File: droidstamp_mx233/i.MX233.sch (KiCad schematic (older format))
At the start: 91 parts, among them IC1 iMX233, J1 MICROSD, J5 JACK-PLUG, P1 CONN_12X2, P10 CONN_1, P2 CONN_12X2, P3 CONN_1, P4 CONN_4X2, P5 CONN_1, P7 CONN_1, Q1 MMDT3904, U1 ADM3101E, U3 M25P32, X1 24MHz

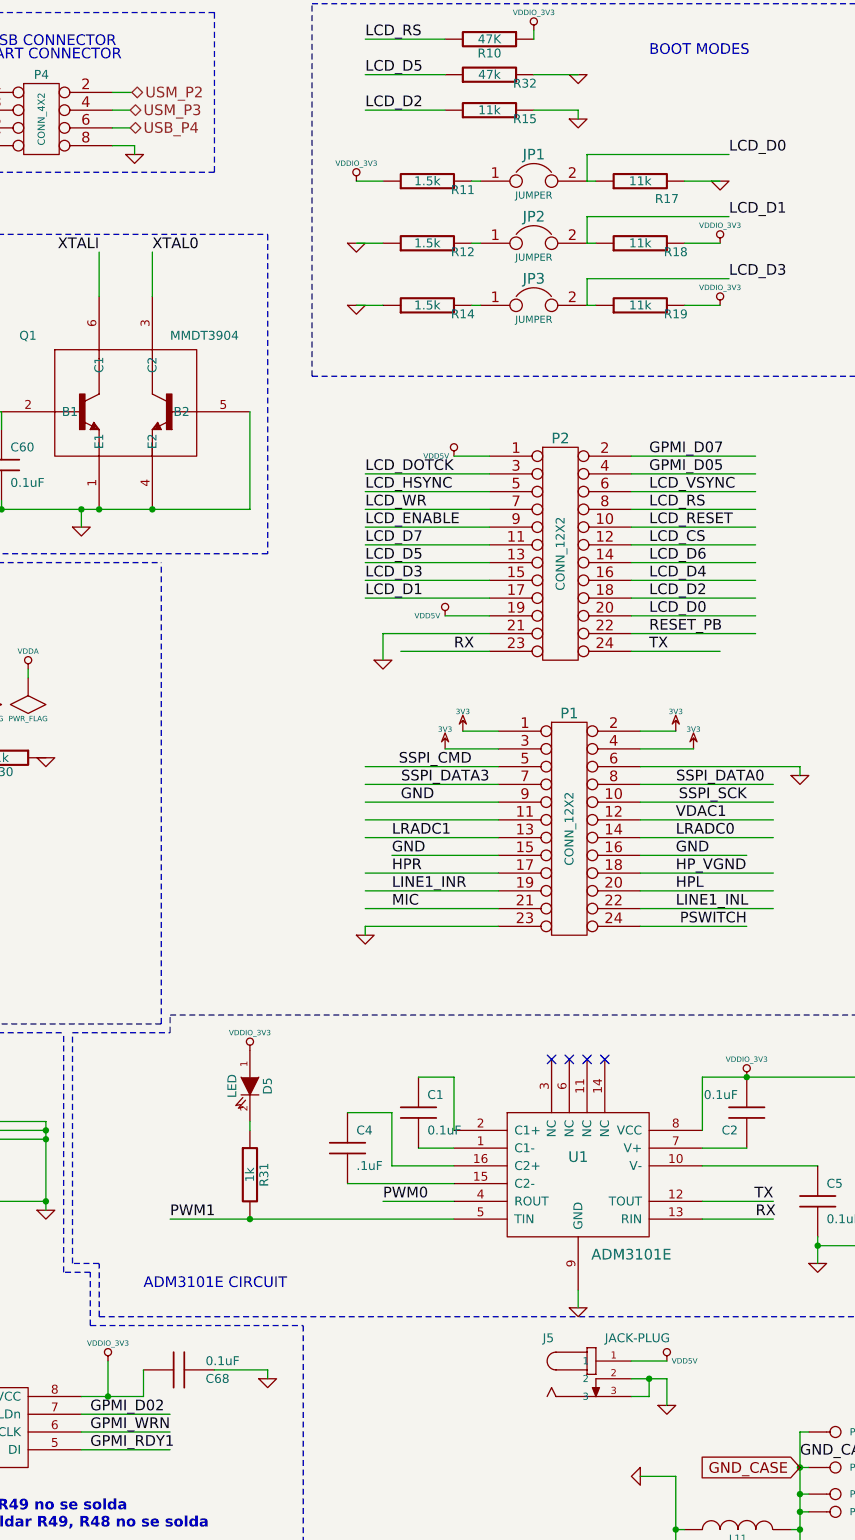
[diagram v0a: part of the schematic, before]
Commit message: fix power jack
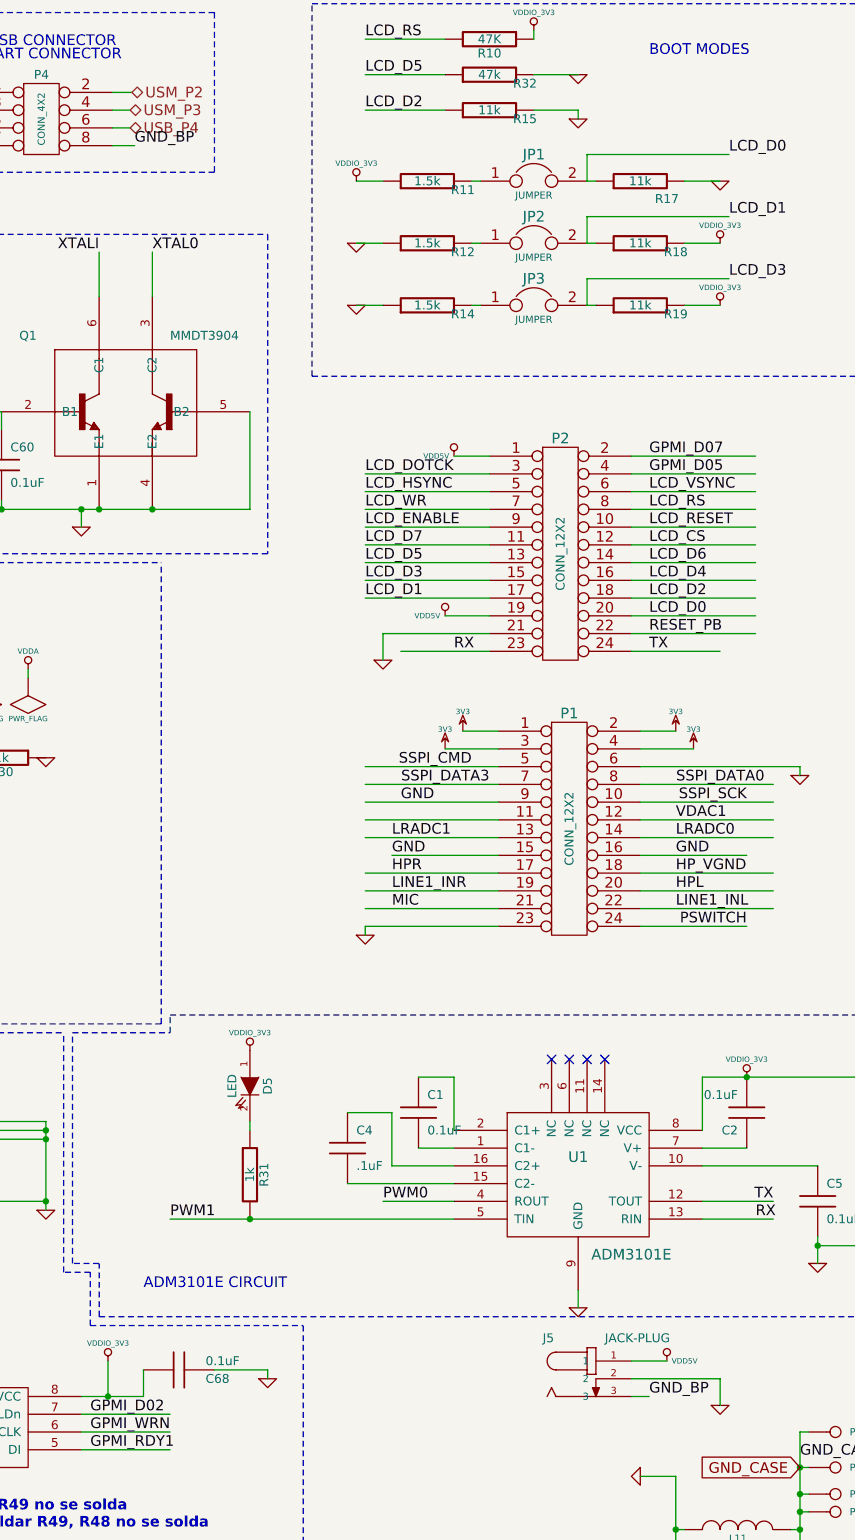
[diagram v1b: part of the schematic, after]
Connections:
- net labels added: GND_BP
- wire segments 402 -> 400
